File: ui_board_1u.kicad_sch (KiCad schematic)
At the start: 38 parts, among them J2 X9555WV-2x06-6TV01, U1 AFC01-S30FCA-00, U4 TPS61040DBV, U6 SPX3819M5-L

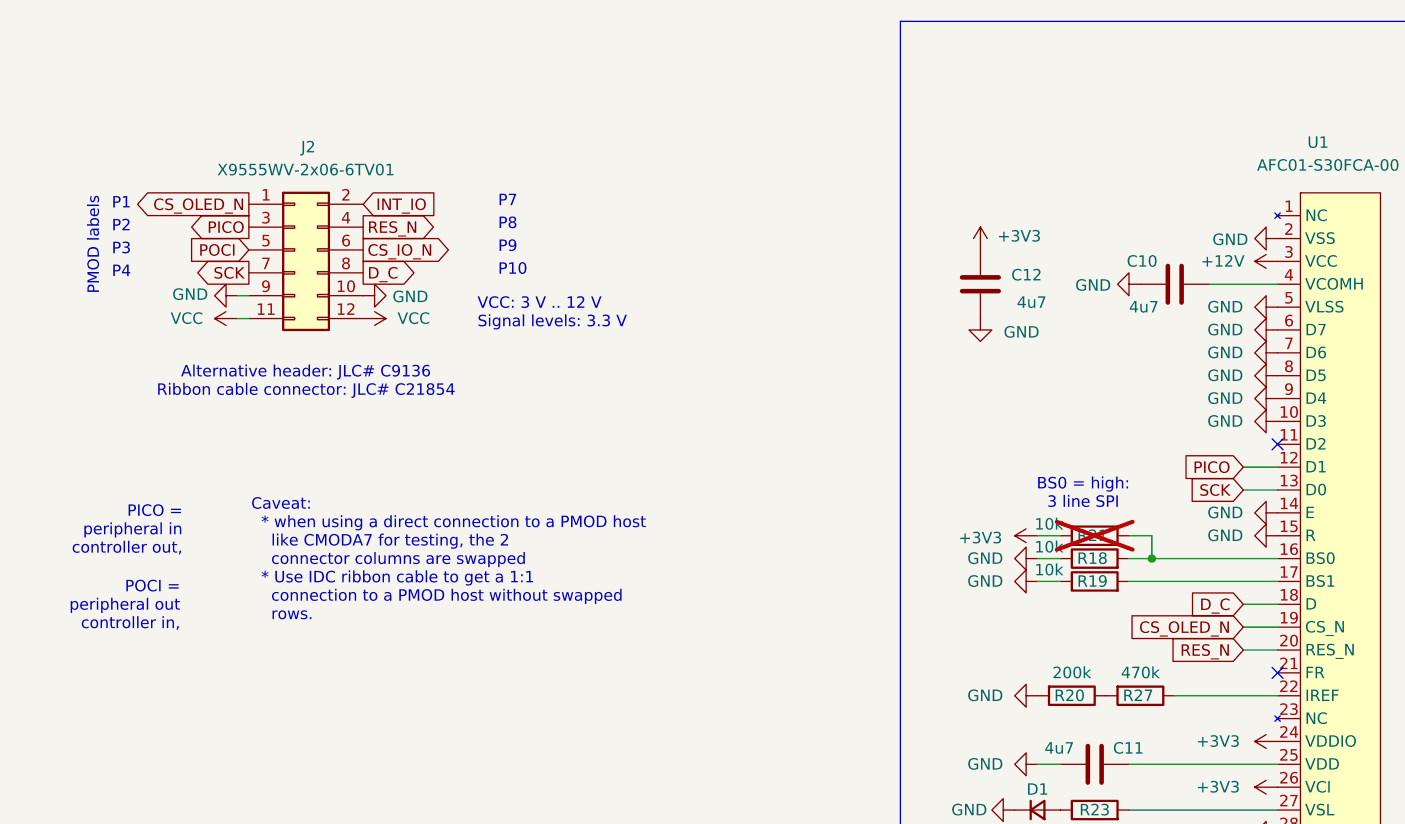
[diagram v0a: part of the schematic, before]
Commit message: rename POCI and PICO signals to SDO and SDI
according to the OSHWA recommendation
https://oshwa.org/resources/a-resolution-to-redefine-spi-signal-names/
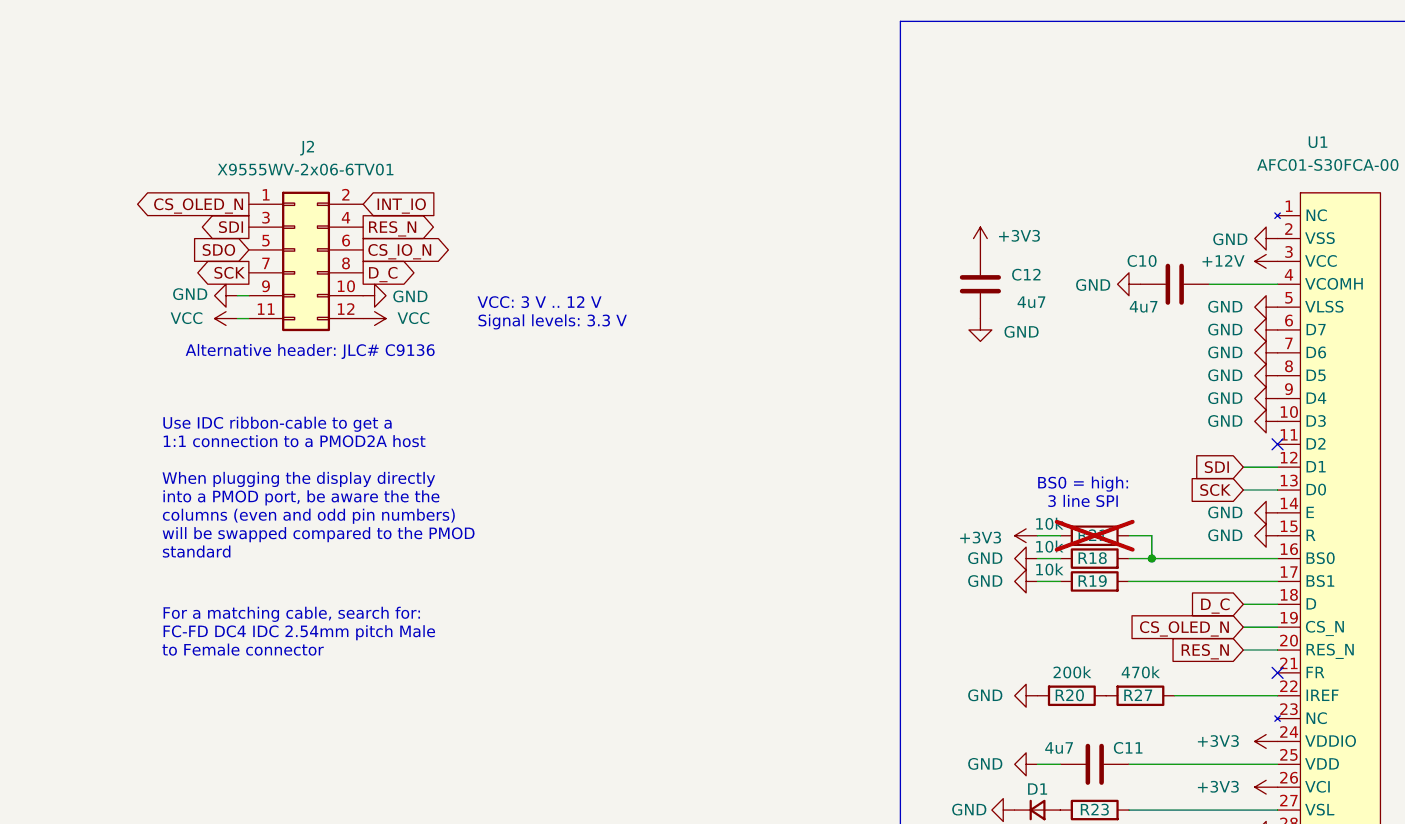
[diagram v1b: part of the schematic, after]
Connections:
- net PICO renamed SDI
- net POCI renamed SDO
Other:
- note added: "Alternative header: JLC# C9136"
- note added: "For a matching cable, search for: FC-FD DC4 IDC 2.54mm pitch Male to Female connector"
- note added: "Use IDC ribbon-cable to get a 1:1 connection to a PMOD2A host When plugging the display directly into a PMOD port, be aware the the columns (even and odd pin numbers) will be swapped compared to the PMOD standard"
- note removed: "Alternative header: JLC# C9136 Ribbon cable connector: JLC# C21854"
- note removed: "Caveat: * when using a direct connection to a PMOD host like CMODA7 for testing, the 2 connector columns are swapped * Use IDC ribbon cable to get a 1:1 connection to a PMOD host without swapped rows."
- note removed: "P1"
- note removed: "P10"
- note removed: "P2"
- note removed: "P3"
- note removed: "P4"
- note removed: "P7"
- note removed: "P8"
- note removed: "P9"
- note removed: "PICO = peripheral in controller out,"
- note removed: "PMOD labels"
- note removed: "POCI = peripheral out controller in,"
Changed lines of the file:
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@@
-		)
-	)
-	(text "P7"
-		(exclude_from_sim no)
-		(at 72.136 53.848 0)
-		(effects
-			(font
-				(size 1.27 1.27)
-			)
-			(justify left bottom)
-		)
-	)
-	(text "P2"
-		(exclude_from_sim no)
-		(at 29.21 56.642 0)
-		(effects
-			(font
-				(size 1.27 1.27)
-			)
-			(justify left bottom)
 		)
 	)
@@
 		)
 	)
-	(text "Alternative header: JLC# C9136\nRibbon cable connector: JLC# C21854"
+	(text "Alternative header: JLC# C9136"
 		(exclude_from_sim no)
-		(at 50.8 73.152 0)
+		(at 51.308 69.85 0)
 		(effects
 			(font
@@
 		)
 	)
-	(text "P4"
+	(text "Use IDC ribbon-cable to get a \n1:1 connection to a PMOD2A host\n\nWhen plugging the display directly\ninto a PMOD port, be aware the the\ncolumns (even and odd pin numbers)\nwill be swapped compared to the PMOD\nstandard\n\n"
 		(exclude_from_sim no)
-		(at 29.21 61.722 0)
-		(effects
-			(font
-				(size 1.27 1.27)
-			)
-			(justify left bottom)
-		)
-	)
-	(text "PICO =\nperipheral in\ncontroller out,\n"
-		(exclude_from_sim no)
-		(at 37.084 92.456 0)
-		(effects
-			(font
-				(size 1.27 1.27)
-			)
-			(justify right bottom)
-		)
-	)
-	(text "Caveat:\n  * when using a direct connection to a PMOD host\n    like CMODA7 for testing, the 2 \n    connector columns are swapped\n  * Use IDC ribbon cable to get a 1:1\n	connection to a PMOD host without swapped\n	rows."
-		(exclude_from_sim no)
-		(at 44.704 92.964 0)
+		(at 34.798 86.106 0)
 		(effects
 			(font
@@
 		)
 	)
+	(text "For a matching cable, search for:\nFC-FD DC4 IDC 2.54mm pitch Male \nto Female connector "
+		(exclude_from_sim no)
+		(at 34.798 101.092 0)
+		(effects
+			(font
+				(size 1.27 1.27)
+			)
+			(justify left)
+		)
+	)
 	(text "BS0 = high:\n3 line SPI"
 		(exclude_from_sim no)
@@
 		)
 	)
-	(text "P9"
-		(exclude_from_sim no)
-		(at 72.136 58.928 0)
-		(effects
-			(font
-				(size 1.27 1.27)
-			)
-			(justify left bottom)
-		)
-	)
-	(text "P1"
-		(exclude_from_sim no)
-		(at 29.21 54.102 0)
-		(effects
-			(font
-				(size 1.27 1.27)
-			)
-			(justify left bottom)
-		)
-	)
-	(text "P3"
-		(exclude_from_sim no)
-		(at 29.21 59.182 0)
-		(effects
-			(font
-				(size 1.27 1.27)
-			)
-			(justify left bottom)
-		)
-	)
-	(text "PMOD labels"
-		(exclude_from_sim no)
-		(at 27.94 63.5 90)
-		(effects
-			(font
-				(size 1.27 1.27)
-			)
-			(justify left bottom)
-		)
-	)
 	(text "VOUT = 1.235V * (1 + R1/R2) = 3.34 V"
 		(exclude_from_sim no)
@@
 			)
 			(justify left)
-		)
-	)
-	(text "POCI = \nperipheral out\ncontroller in,\n"
-		(exclude_from_sim no)
-		(at 36.83 100.838 0)
-		(effects
-			(font
-				(size 1.27 1.27)
-			)
-			(justify right bottom)
-		)
-	)
-	(text "P10"
-		(exclude_from_sim no)
-		(at 72.136 61.468 0)
-		(effects
-			(font
-				(size 1.27 1.27)
-			)
-			(justify left bottom)
-		)
-	)
-	(text "P8"
-		(exclude_from_sim no)
-		(at 72.136 56.388 0)
-		(effects
-			(font
-				(size 1.27 1.27)
-			)
-			(justify left bottom)
 		)
 	)
@@
 			"a51VAABoreprnVUAAGCs6mudVQAAuKzqa51VAABwruprnVUAAMiu6mudVQAAwK3qa51VAAAYrupr"
 			"nVUAADCm6mudVQAAiKbqa51VAADQr+prnVUAACiw6mudVQAAIK/qa51VAAB4r+prnVUAAICw6mud"
-			"VQAA2LDqa51VAA=="
+			"VQAA2LDqa51VAAAAAAAAAAAAAAAAAAAAAAAAAAAAAAAAAAAAAAAAAAAAAAAAAAAAAAAAAAAAAAAA"
+			"AAAAAAAAAAAAAAAAAAAAAAAAAAAAAAAAAAAAAAAAAAAAAAAAAAAAAAAAAAAAAAAAAAAAAAAAAAAA"
+			"AAAAAAAAAAAAAAAAAAAAAAAAAAAAAAAAAAAAAAAAAAAAAAAAAAAAAAAAAAAAAAAAAAAAAAAAAAAA"
+			"AAAAAAAAAAAAAAAAAAAAAAAAAAAAAAAAAAAAAAAAAAAAAAAAAAAAAAAAAAAAAAAAAAAAAAAAAAAA"
+			"AAAAAAAAAAAAAAAAAAAAAAAAAAAAAAAAAAAAAAAAAAAAAAAAAAAAAAAAAAAAAAAAAAAAAAAAAAAA"
+			"AAAAAAAAAAAAAAAAAAAAAAAAAAAAAAAAAAAAAAAAAAAAAAAAAAAAAAAAAAAAAAAAAAAAAAAAAAAA"
+			"AAAAAAAAAAAAAAAAAAAAAAAAAAAAAAAAAAAAAAAAAAAAAAAAAAAAAAAAAAAAAAAAAAAAAAAAAAAA"
+			"AAAAAAAAAAAAAAAAAAAAAAAAAAAAAAAAAAAAAAAAAAAAAAAAAAAAAAAAAAAAAAAAAAAAAAAAAAAA"
+			"AAAAAAAAAAAAAAAAAAAAAAAAAAAAAAAAAAAAAAAAAAAAAAAAAAAAAAAAAAAAAAAAAAAAAAAAAAAA"
+			"AAAAAAAAAAAAAAAAAAAAAAAAAAAAAAAAAAAAAAAAAAAAAAAAAAAAAAAAAAAAAAAAAAAAAAAAAAAA"
+			"AAAAAAAAAAAAAAAAAAAAAAAAAAAAAAAAAAAAAAAAAAAAAAAAAAAAAAAAAAAAAAAAAAAAAAAAAAAA"
+			"AAAAAAAAAAAAAAAAAAAAAAAAAAAAAAAAAAAAAAAAAAAAAAAAAAAAAAAAAAAAAAAAAAAAAAAAAAAA"
+			"AAAAAAAAAAAAAAAAAAAAAAAAAAAAAAAAAAAAAAAAAAAAAAAAAAAAAAAAAAAAAAAAAAAAAAAAAAAA"
+			"AAAAAAAAAAAAAAAAAAAAAAAAAAAAAAAAAAAAAAAAAAAAAAAAAAAAAAAAAAAAAAAAAAAAAAAAAAAA"
+			"AAAAAAAAAAAAAAAAAAAAAAAAAAAAAAAAAAAAAAAAAAAAAAAAAAAAAAAAAAAAAAAAAAAAAAAAAAAA"
+			"AAAAAAAAAAAAAAAAAAAAAAAAAAAAAAAAAAAAAAAAAAAAAAAAAAAAAAAAAAAAAAAAAAAAAAAAAAAA"
+			"AAAAAAAAAAAAAAAAAAAAAAAAAAAAAAAAAAAAAAAAAAAAAAAAAAAAAAAAAAAAAAAAAAAAAAAAAAAA"
+			"AAAAAAAAAAAAAAAAAAAAAAAAAAAAAAAAAAAAAAAAAAAAAAAAAAAAAAAAAAAAAAAAAAAAAAAAAAAA"
+			"AAAAAAAAAAAAAA=="
 		)
 	)
@@
 		)
 	)
-	(global_label "POCI"
+	(global_label "SDO"
 		(shape input)
 		(at 44.45 58.42 180)
@@
 		)
 		(property "Intersheetrefs" "${INTERSHEET_REFS}"
-			(at 37.6437 58.42 0)
+			(at 38.309 58.42 0)
 			(effects
 				(font
@@
 		)
 	)
-	(global_label "PICO"
+	(global_label "SDI"
 		(shape output)
 		(at 44.45 55.88 180)
@@
 		)
 		(property "Intersheetrefs" "${INTERSHEET_REFS}"
-			(at 37.6437 55.88 0)
+			(at 39.0347 55.88 0)
 			(effects
 				(font
@@
 		)
 	)
-	(global_label "PICO"
+	(global_label "SDI"
 		(shape input)
 		(at 154.94 82.55 180)
@@
 		)
 		(property "Intersheetrefs" "${INTERSHEET_REFS}"
-			(at 148.1337 82.55 0)
+			(at 149.5247 82.55 0)
 			(effects
 				(font

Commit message: geographical re-annotate
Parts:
- renumbered C15 to C1, C8 to C15, C12 to C2, C10 to C3, C2 to C4, C9 to C5, C1 to C6, C11 to C7, C14 to C8, C17 to C9, D1 to D3, D5 to D4, H5 to H1, H6 to H12, H1 to H16, H2 to H17, H3 to H21, H4 to H22, H7 to H32, H8 to H40, J2 to J1, R42 to R1, R20 to R10, R45 to R2, R7 to R3, R22 to R4, R23 to R5, R19 to R6, R18 to R7, R21 to R8, R27 to R9, U6 to U2, U4 to U3
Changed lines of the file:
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@@
 		(on_board yes)
 		(dnp no)
-		(property "Reference" "C2"
+		(property "Reference" "C4"
 			(at 205.232 122.936 0)
 			(effects
@@
 			(project ""
 				(path "/3def8ca7-c7ff-40fd-acc8-d6d3f6c3eb5b"
-					(reference "C2")
+					(reference "C4")
 					(unit 1)
 				)
@@
 		(on_board yes)
 		(dnp no)
-		(property "Reference" "R7"
+		(property "Reference" "R3"
 			(at 147.828 166.878 0)
 			(effects
@@
 			(project ""
 				(path "/3def8ca7-c7ff-40fd-acc8-d6d3f6c3eb5b"
-					(reference "R7")
+					(reference "R3")
 					(unit 1)
 				)
@@
 		(on_board yes)
 		(dnp no)
-		(property "Reference" "J2"
+		(property "Reference" "J1"
 			(at 51.054 46.99 0)
 			(effects
@@
 			(project ""
 				(path "/3def8ca7-c7ff-40fd-acc8-d6d3f6c3eb5b"
-					(reference "J2")
+					(reference "J1")
 					(unit 1)
 				)
@@
 		(on_board yes)
 		(dnp no)
-		(property "Reference" "D1"
+		(property "Reference" "D3"
 			(at 132.08 118.364 0)
 			(effects
@@
 			(project ""
 				(path "/3def8ca7-c7ff-40fd-acc8-d6d3f6c3eb5b"
-					(reference "D1")
+					(reference "D3")
 					(unit 1)
 				)
@@
 		(on_board yes)
 		(dnp yes)
-		(property "Reference" "R21"
+		(property "Reference" "R8"
 			(at 138.176 90.17 90)
 			(effects
@@
 			(project "ui_board_1u"
 				(path "/3def8ca7-c7ff-40fd-acc8-d6d3f6c3eb5b"
-					(reference "R21")
+					(reference "R8")
 					(unit 1)
 				)
@@
 		(on_board yes)
 		(dnp no)
-		(property "Reference" "R45"
+		(property "Reference" "R2"
 			(at 245.11 93.98 90)
 			(effects
@@
 			(project "ui_board_1u"
 				(path "/3def8ca7-c7ff-40fd-acc8-d6d3f6c3eb5b"
-					(reference "R45")
+					(reference "R2")
 					(unit 1)
 				)
@@
 		(on_board yes)
 		(dnp no)
-		(property "Reference" "C11"
+		(property "Reference" "C7"
 			(at 140.462 113.792 90)
 			(effects
@@
 			(project "ui_board_1u"
 				(path "/3def8ca7-c7ff-40fd-acc8-d6d3f6c3eb5b"
-					(reference "C11")
+					(reference "C7")
 					(unit 1)
 				)
@@
 		(dnp no)
 		(fields_autoplaced yes)
-		(property "Reference" "H3"
+		(property "Reference" "H21"
 			(at 269.24 168.9099 0)
 			(effects
@@
 			(project "ui_board_1u"
 				(path "/3def8ca7-c7ff-40fd-acc8-d6d3f6c3eb5b"
-					(reference "H3")
+					(reference "H21")
 					(unit 1)
 				)
@@
 		(on_board yes)
 		(dnp no)
-		(property "Reference" "R42"
+		(property "Reference" "R1"
 			(at 245.11 86.614 90)
 			(effects
@@
 			(project "ui_board_1u"
 				(path "/3def8ca7-c7ff-40fd-acc8-d6d3f6c3eb5b"
-					(reference "R42")
+					(reference "R1")
 					(unit 1)
 				)
@@
 		(on_board yes)
 		(dnp no)
-		(property "Reference" "R22"
+		(property "Reference" "R4"
 			(at 158.75 166.624 0)
 			(effects
@@
 			(project "ui_board_1u"
 				(path "/3def8ca7-c7ff-40fd-acc8-d6d3f6c3eb5b"
-					(reference "R22")
+					(reference "R4")
 					(unit 1)
 				)
@@
 		(on_board yes)
 		(dnp no)
-		(property "Reference" "R18"
+		(property "Reference" "R7"
 			(at 138.176 92.71 90)
 			(effects
@@
 			(project "ui_board_1u"
 				(path "/3def8ca7-c7ff-40fd-acc8-d6d3f6c3eb5b"
-					(reference "R18")
+					(reference "R7")
 					(unit 1)
 				)
@@
 		(on_board yes)
 		(dnp no)
-		(property "Reference" "C12"
+		(property "Reference" "C2"
 			(at 132.588 61.214 0)
 			(effects
@@
 			(project "ui_board_1u"
 				(path "/3def8ca7-c7ff-40fd-acc8-d6d3f6c3eb5b"
-					(reference "C12")
+					(reference "C2")
 					(unit 1)
 				)
@@
 		(dnp no)
 		(fields_autoplaced yes)
-		(property "Reference" "H2"
+		(property "Reference" "H17"
 			(at 259.08 168.9099 0)
 			(effects
@@
 			(project "ui_board_1u"
 				(path "/3def8ca7-c7ff-40fd-acc8-d6d3f6c3eb5b"
-					(reference "H2")
+					(reference "H17")
 					(unit 1)
 				)
@@
 		(on_board yes)
 		(dnp no)
-		(property "Reference" "C14"
+		(property "Reference" "C8"
 			(at 257.556 123.19 0)
 			(effects
@@
 			(project "ui_board_1u"
 				(path "/3def8ca7-c7ff-40fd-acc8-d6d3f6c3eb5b"
-					(reference "C14")
+					(reference "C8")
 					(unit 1)
 				)
@@
 		(on_board yes)
 		(dnp no)
-		(property "Reference" "C1"
+		(property "Reference" "C6"
 			(at 198.882 122.936 0)
 			(effects
@@
 			(project "ui_board_1u"
 				(path "/3def8ca7-c7ff-40fd-acc8-d6d3f6c3eb5b"
-					(reference "C1")
+					(reference "C6")
 					(unit 1)
 				)
@@
 		(on_board yes)
 		(dnp no)
-		(property "Reference" "C8"
-			(at 245.618 123.444 0)
+		(property "Reference" "C15"
+			(at 244.602 123.444 0)
 			(effects
 				(font
@@
 			(project "ui_board_1u"
 				(path "/3def8ca7-c7ff-40fd-acc8-d6d3f6c3eb5b"
-					(reference "C8")
+					(reference "C15")
 					(unit 1)
 				)
@@
 		(dnp no)
 		(fields_autoplaced yes)
-		(property "Reference" "H8"
+		(property "Reference" "H40"
 			(at 279.4 175.2599 0)
 			(effects
@@
 			(project "ui_board_1u"
 				(path "/3def8ca7-c7ff-40fd-acc8-d6d3f6c3eb5b"
-					(reference "H8")
+					(reference "H40")
 					(unit 1)
 				)
@@
 		(on_board yes)
 		(dnp no)
-		(property "Reference" "C15"
+		(property "Reference" "C1"
 			(at 251.206 87.63 0)
 			(effects
@@
 			(project "ui_board_1u"
 				(path "/3def8ca7-c7ff-40fd-acc8-d6d3f6c3eb5b"
-					(reference "C15")
+					(reference "C1")
 					(unit 1)
 				)
@@
 		(on_board yes)
 		(dnp no)
-		(property "Reference" "R23"
+		(property "Reference" "R5"
 			(at 138.43 120.65 90)
 			(effects
@@
 			(project "ui_board_1u"
 				(path "/3def8ca7-c7ff-40fd-acc8-d6d3f6c3eb5b"
-					(reference "R23")
+					(reference "R5")
 					(unit 1)
 				)
@@
 		(on_board yes)
 		(dnp no)
-		(property "Reference" "R20"
+		(property "Reference" "R10"
 			(at 135.636 107.95 90)
 			(effects
@@
 			(project "ui_board_1u"
 				(path "/3def8ca7-c7ff-40fd-acc8-d6d3f6c3eb5b"
-					(reference "R20")
+					(reference "R10")
 					(unit 1)
 				)
@@
 		(on_board yes)
 		(dnp no)
-		(property "Reference" "U4"
+		(property "Reference" "U3"
 			(at 213.868 134.112 0)
 			(effects
@@
 			(project ""
 				(path "/3def8ca7-c7ff-40fd-acc8-d6d3f6c3eb5b"
-					(reference "U4")
+					(reference "U3")
 					(unit 1)
 				)
@@
 		(dnp no)
 		(fields_autoplaced yes)
-		(property "Reference" "H7"
+		(property "Reference" "H32"
 			(at 269.24 175.2599 0)
 			(effects
@@
 			(project "ui_board_1u"
 				(path "/3def8ca7-c7ff-40fd-acc8-d6d3f6c3eb5b"
-					(reference "H7")
+					(reference "H32")
 					(unit 1)
 				)
@@
 		(dnp no)
 		(fields_autoplaced yes)
-		(property "Reference" "H1"
+		(property "Reference" "H16"
 			(at 248.92 168.9099 0)
 			(effects
@@
 			(project ""
 				(path "/3def8ca7-c7ff-40fd-acc8-d6d3f6c3eb5b"
-					(reference "H1")
+					(reference "H16")
 					(unit 1)
 				)
@@
 		(dnp no)
 		(fields_autoplaced yes)
-		(property "Reference" "H4"
+		(property "Reference" "H22"
 			(at 279.4 168.9099 0)
 			(effects
@@
 			(project "ui_board_1u"
 				(path "/3def8ca7-c7ff-40fd-acc8-d6d3f6c3eb5b"
-					(reference "H4")
+					(reference "H22")
 					(unit 1)
 				)
@@
 		(on_board yes)
 		(dnp no)
-		(property "Reference" "C10"
+		(property "Reference" "C3"
 			(at 141.986 59.69 90)
 			(effects
@@
 			(project "ui_board_1u"
 				(path "/3def8ca7-c7ff-40fd-acc8-d6d3f6c3eb5b"
-					(reference "C10")
+					(reference "C3")
 					(unit 1)
 				)
@@
 		(on_board yes)
 		(dnp no)
-		(property "Reference" "R19"
+		(property "Reference" "R6"
 			(at 138.176 95.25 90)
 			(effects
@@
 			(project "ui_board_1u"
 				(path "/3def8ca7-c7ff-40fd-acc8-d6d3f6c3eb5b"
-					(reference "R19")
+					(reference "R6")
 					(unit 1)
 				)
@@
 		(dnp no)
 		(fields_autoplaced yes)
-		(property "Reference" "H6"
+		(property "Reference" "H12"
 			(at 259.08 175.2599 0)
 			(effects
@@
 			(project "ui_board_1u"
 				(path "/3def8ca7-c7ff-40fd-acc8-d6d3f6c3eb5b"
-					(reference "H6")
+					(reference "H12")
 					(unit 1)
 				)
@@
 		(on_board yes)
 		(dnp no)
-		(property "Reference" "R27"
+		(property "Reference" "R9"
 			(at 143.256 107.95 90)
 			(effects
@@
 			(project "ui_board_1u"
 				(path "/3def8ca7-c7ff-40fd-acc8-d6d3f6c3eb5b"
-					(reference "R27")
+					(reference "R9")
 					(unit 1)
 				)
@@
 		(dnp no)
 		(fields_autoplaced yes)
-		(property "Reference" "H5"
+		(property "Reference" "H1"
 			(at 248.92 175.2599 0)
 			(effects
@@
 			(project "ui_board_1u"
 				(path "/3def8ca7-c7ff-40fd-acc8-d6d3f6c3eb5b"
-					(reference "H5")
+					(reference "H1")
 					(unit 1)
 				)
@@
 		(on_board yes)
 		(dnp no)
-		(property "Reference" "D5"
+		(property "Reference" "D4"
 			(at 234.95 123.444 0)
 			(effects
@@
 			(project ""
 				(path "/3def8ca7-c7ff-40fd-acc8-d6d3f6c3eb5b"
-					(reference "D5")
+					(reference "D4")
 					(unit 1)
 				)
@@
 		(on_board yes)
 		(dnp no)
-		(property "Reference" "C9"
+		(property "Reference" "C5"
 			(at 252.222 123.19 0)
 			(effects
@@
 			(project "ui_board_1u"
 				(path "/3def8ca7-c7ff-40fd-acc8-d6d3f6c3eb5b"
-					(reference "C9")
+					(reference "C5")
 					(unit 1)
 				)
@@
 		(dnp no)
 		(fields_autoplaced yes)
-		(property "Reference" "U6"
+		(property "Reference" "U2"
 			(at 222.25 76.2 0)
 			(effects
@@
 			(project "ui_board_1u"
 				(path "/3def8ca7-c7ff-40fd-acc8-d6d3f6c3eb5b"
-					(reference "U6")
+					(reference "U2")
 					(unit 1)
 				)
@@
 		(on_board yes)
 		(dnp no)
-		(property "Reference" "C17"
+		(property "Reference" "C9"
 			(at 200.406 86.36 0)
 			(effects
@@
 			(project "ui_board_1u"
 				(path "/3def8ca7-c7ff-40fd-acc8-d6d3f6c3eb5b"
-					(reference "C17")
+					(reference "C9")
 					(unit 1)
 				)
